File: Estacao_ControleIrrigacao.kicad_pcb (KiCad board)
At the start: 2 copper layers, 140 x 70 mm, 19 parts, among them J1 Screw_Terminal_01x09, J10 Conn_01x06_Socket, J2 Screw_Terminal_01x09, J3 Screw_Terminal_01x09, J4 Screw_Terminal_01x09, J5 HALL1_Terminal_01x03, J6 HALL2_Terminal_01x03, J7 SHT_Terminal_01x04, J8 DHT_Terminal_01x03, J9 Conn_01x06_Socket, U1 WIFI_KIT_32__V3_

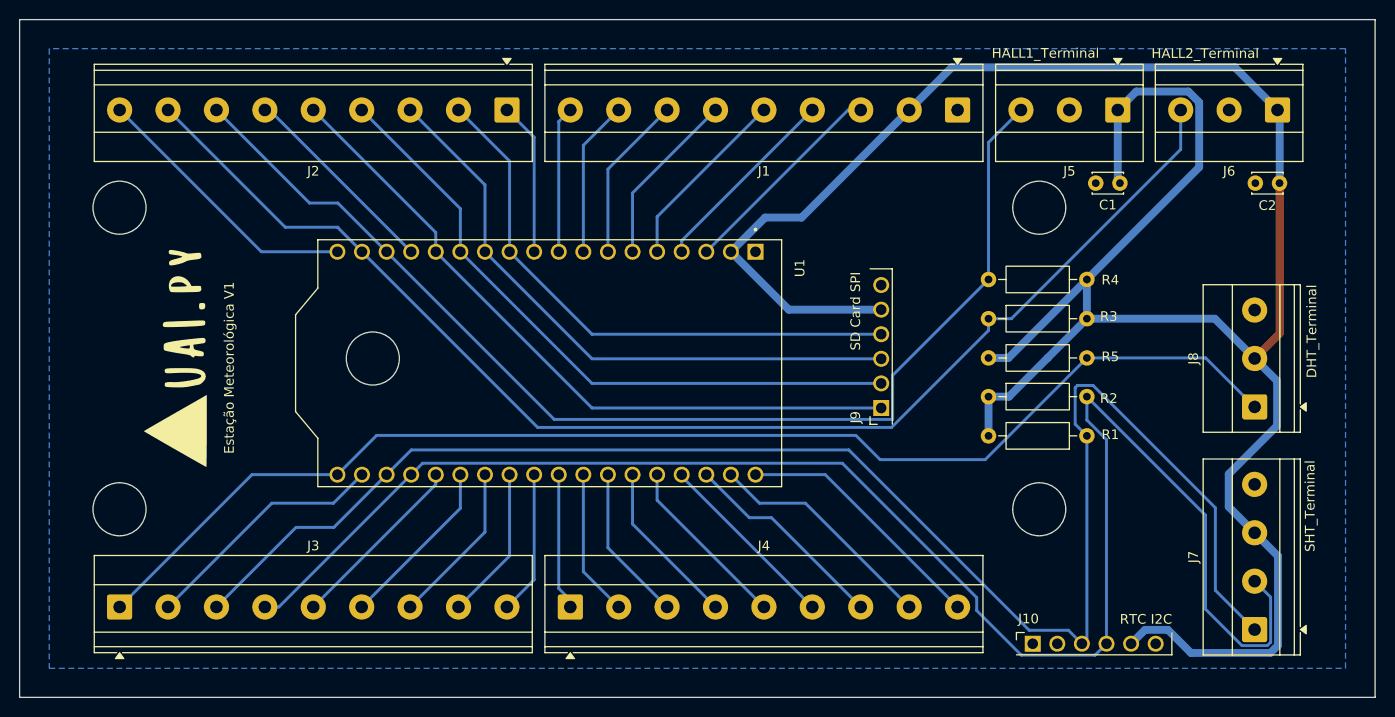
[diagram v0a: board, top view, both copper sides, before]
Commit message: docs: update silkscreen with esp pin labels
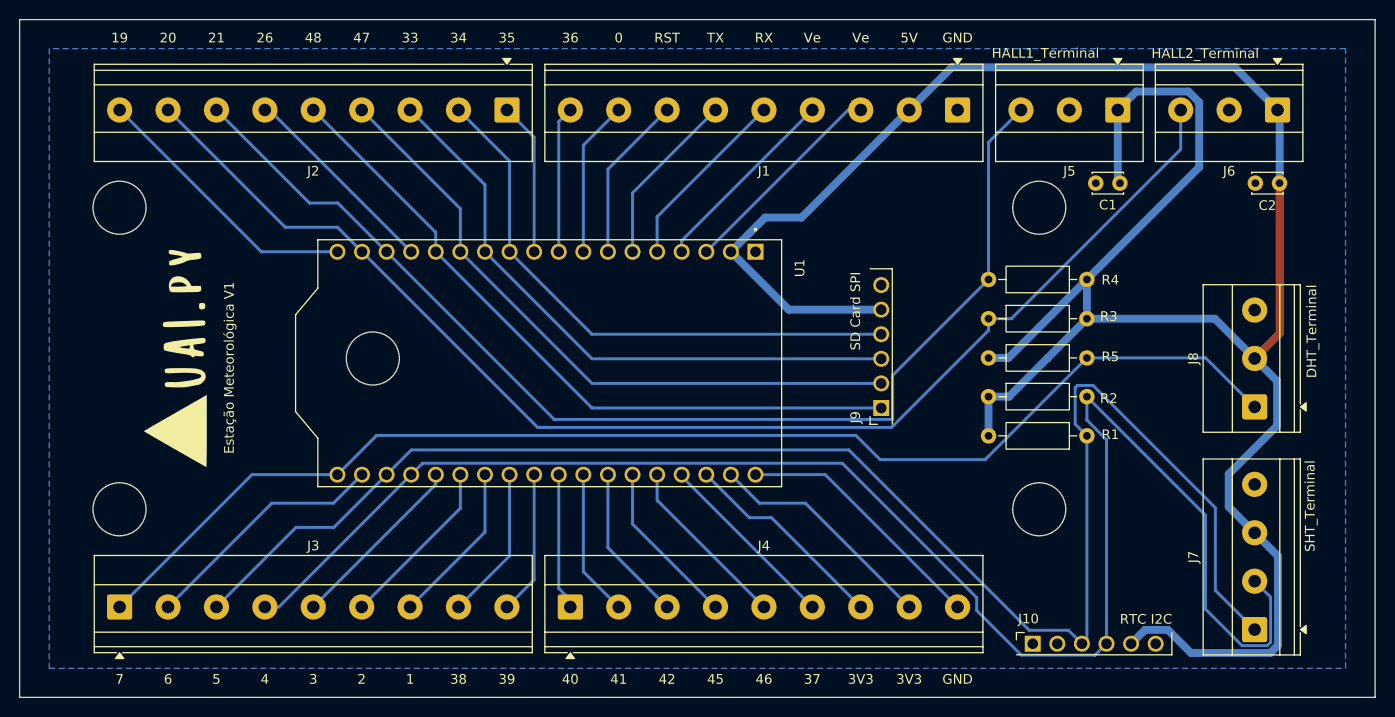
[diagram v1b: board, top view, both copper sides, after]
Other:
- board text added: "0"
- board text added: "1"
- board text added: "19"
- board text added: "2"
- board text added: "20"
- board text added: "21"
- board text added: "26"
- board text added: "3"
- board text added: "33"
- board text added: "34"
- board text added: "35"
- board text added: "36"
- board text added: "37"
- board text added: "38"
- board text added: "39"
- board text added: "3V3"
- board text added: "4"
- board text added: "40"
- board text added: "41"
- board text added: "42"
- board text added: "45"
- board text added: "46"
- board text added: "47"
- board text added: "48"
- board text added: "5"
- board text added: "5V"
- board text added: "6"
- board text added: "7"
- board text added: "GND"
- board text added: "RST"
- board text added: "RX"
- board text added: "TX"
- board text added: "Ve"
